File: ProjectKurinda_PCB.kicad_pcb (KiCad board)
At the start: 2 copper layers, 30 x 105 mm, 9 parts, among them J1 JST PH, U1 ESP32-C3 SUPERMINI, U2 DHT11 T&H module, U3 Water sensor module, U4 SD3031 RTC module, U5 MPU6050 accelerometer module

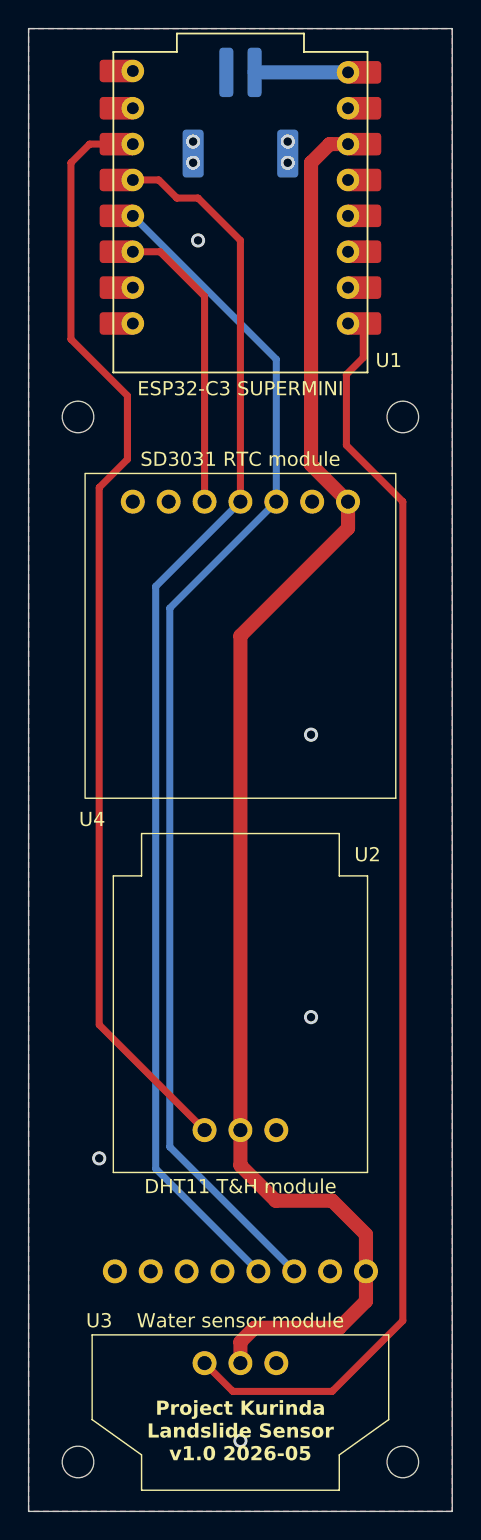
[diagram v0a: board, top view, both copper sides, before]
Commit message: New version v1.1 of sensor PCB with new sensor modules and extra features, and updated README file.
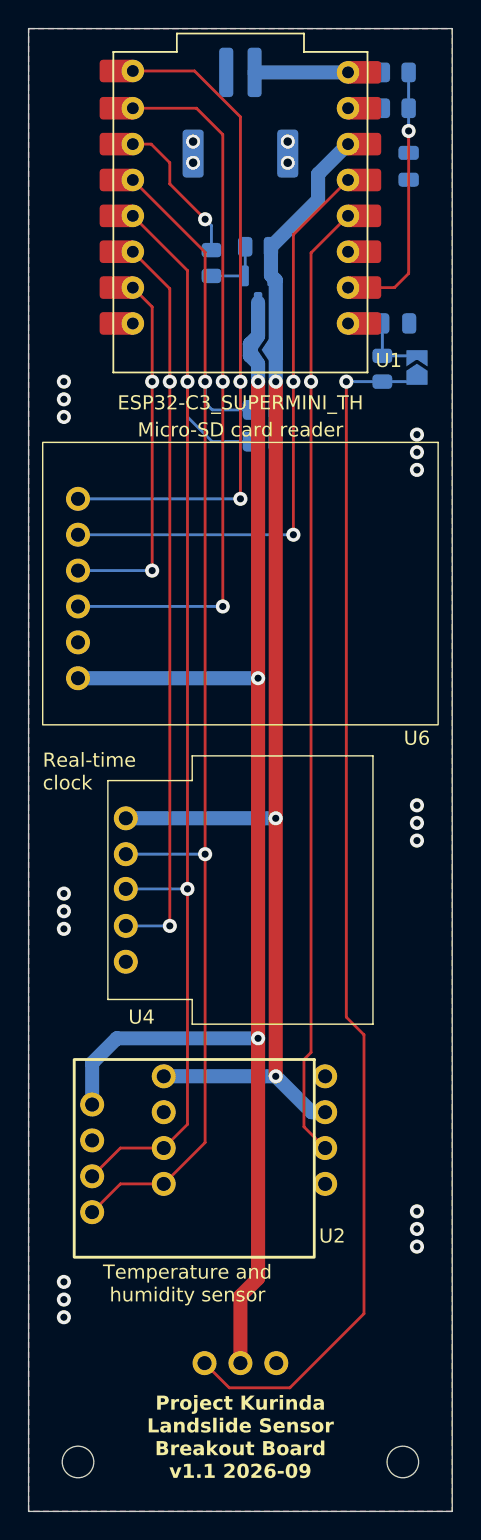
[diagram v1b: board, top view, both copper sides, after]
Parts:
- removed REF**: KiCad-Logo_5mm_SilkScreen, Symbol:KiCad-Logo_5mm_SilkScreen
- removed REF**: OSHW-Logo_7.5x8mm_SilkScreen, Symbol:OSHW-Logo_7.5x8mm_SilkScreen
- added C1: 1uF, Capacitor_SMD:C_0805_2012Metric, B.Cu at (81.0, 65.9)
- added C2: 1uF, Capacitor_SMD:C_0805_2012Metric, B.Cu at (81.9, 54.8)
- added JP1: Jumper_2_Open, Jumper:SolderJumper-2_P1.3mm_Open_TrianglePad1.0x1.5mm, B.Cu at (71.8, 67.8)
- added JP2: Jumper_2_Open, Jumper:SolderJumper-2_P1.3mm_Open_TrianglePad1.0x1.5mm, B.Cu at (82.5, 69.0)
- added Q2: Q_PMOS_GSD, Package_TO_SOT_SMD:SOT-23, B.Cu at (71.2, 63.5)
- added R1: 300 kR, Resistor_SMD:R_0805_2012Metric, B.Cu at (81.0, 48.1)
- added R2: 100 kR, Resistor_SMD:R_0805_2012Metric, B.Cu at (81.0, 50.6)
- added R3: 1 kR, Resistor_SMD:R_0805_2012Metric, B.Cu at (68.0, 61.6)
- added R4: 100 kR, Resistor_SMD:R_0805_2012Metric, B.Cu at (71.2, 60.5)
- added R5: 1kR, Resistor_SMD:R_0805_2012Metric, B.Cu at (80.0, 69.1)
- added R6: 4.7kR, Resistor_SMD:R_0805_2012Metric, B.Cu at (71.6, 72.0)
- added R7: 4.7kR, Resistor_SMD:R_0805_2012Metric, B.Cu at (71.6, 74.2)
- added U6: ~, ProjectKurinda_PCB_footprints:uSD breakout, F.Cu at (58.5, 84.7)
- J1: value JST PH -> Conn_01x02
- U1: value ESP32-C3 SUPERMINI -> ESP32-C3_SUPERMINI_TH
- U2: value DHT11 T&H module -> SHT40; footprint ProjectKurinda_PCB_footprints:DHT11 -> ProjectKurinda_PCB_footprints:SHT40
- U3: value Water sensor module -> Water Sensor; moved to B.Cu
- U4: value SD3031 RTC module -> RV3028 RTC; footprint ProjectKurinda_PCB_footprints:SD3031 RTC -> ProjectKurinda_PCB_footprints:RV3028 RTC breakout
- U5: value MPU6050 accelerometer module -> LIS2DW12 breakout; footprint ProjectKurinda_PCB_footprints:MPU6050 -> ProjectKurinda_PCB_footprints:LIS2DW12 breakout
- moved U4 28.7 mm to (61.9, 106.0), turned to -90 degrees
- moved G*** 14.1 mm to (71.8, 89.0)
- moved U5 11.7 mm to (76.0, 123.0), turned to -90 degrees
- moved U2 10.7 mm to (59.5, 125.0), turned to -90 degrees
- turned U3 to 180 degrees
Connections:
- net +5V renamed +BATT
- U1 pad 0: /WS_AOUT -> Net-(JP2-B)
- U1 pad 1: unconnected-(U1-GPIO1-Pad1) -> /BAT_MEAS
- U1 pad 20: unconnected-(U1-GPIO20-Pad20)_1 -> /CS
- U1 pad 3: unconnected-(U1-GPIO3-Pad3) -> /MPU_INT1
- U1 pad 4: unconnected-(U1-GPIO4-Pad4)_1 -> /SCK
- U1 pad 5: unconnected-(U1-GPIO5-Pad5)_1 -> /MISO
- U1 pad 6: unconnected-(U1-GPIO6-Pad6)_1 -> /MOSI
- U1 pad 7: /DHT_1W -> /3V3_EN
- U2 pad 1: /DHT_1W -> /3V3_SWITCHED
- U2 pad 2: +3V3 -> GND
- U2 pad 3: GND -> /SCL
- U3 pad 2: +3V3 -> /3V3_SWITCHED
- U4 pad 2: GND -> /SDA
- U4 pad 4: /SDA -> /RTC_INT
- U4 pad 5: /RTC_INT -> GND
- U5 pad 1: +3V3 -> unconnected-(U5-SDO-Pad1)
- U5 pad 2: GND -> +3V3
- U5 pad 3: /SCL -> /MPU_INT1
- U5 pad 4: /SDA -> unconnected-(U5-INT2-Pad4)
- U5 pad 5: unconnected-(U5-XDA-Pad5) -> /SDA
- U5 pad 6: unconnected-(U5-XCL-Pad6) -> /SCL
- U5 pad 7: unconnected-(U5-AD0-Pad7) -> GND
- U5 pad 8: unconnected-(U5-INT-Pad8) -> +3V3
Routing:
- net /3V3_SWITCHED: track 0.00 -> 104.3 mm, vias 0 -> 3
- net /DHT_1W: track 79.0 -> 0.00 mm
- net /MPU_INT1: track 0.00 -> 67.9 mm, vias 0 -> 1
- net /MOSI: track 0.00 -> 50.9 mm, vias 0 -> 2
- net /MISO: track 0.00 -> 47.2 mm, vias 0 -> 2
- net /SCK: track 0.00 -> 42.0 mm, vias 0 -> 2
- net /RTC_INT: track 20.9 -> 51.9 mm, vias 0 -> 2
- net /CS: track 0.00 -> 26.0 mm, vias 0 -> 2
- net /BAT_MEAS: track 0.00 -> 19.4 mm, vias 0 -> 1
- net /3V3_EN: track 0.00 -> 10.6 mm, vias 0 -> 1
- net +3V3: track 105.6 -> 95.8 mm, vias 0 -> 3
- net Net-(JP2-B): track 0.00 -> 7.39 mm
- net Net-(Q2-G): track 0.00 -> 4.43 mm
- net /WS_AOUT: track 89.7 -> 85.8 mm, vias 0 -> 1
- net /SDA: track 87.9 -> 90.8 mm, vias 0 -> 2
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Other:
- outline, holes or cut-outs redrawn
- board text added: "3.3 V switch"
- board text added: "Accelerometer"
- board text added: "Battery input"
- board text added: "Battery monitor"
- board text added: "Generously sponsored by"
- board text added: "Instructions at kurinda.space"
- board text added: "Micro-SD card reader"
- board text added: "Project Kurinda Landslide Sensor Breakout Board v1.1 2026-09"
- board text added: "Real-time clock"
- board text added: "Temperature and humidity sensor"
- board text added: "i2c pull-ups"
- board text removed: "Generously sponsored by:"
- board text removed: "Project Kurinda Landslide Sensor v1.0 2026-05"
